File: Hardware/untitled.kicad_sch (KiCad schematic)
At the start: 16 parts, among them IC1 LM74502HDDFR, J3 CarLVPowerConnector, Q12 PSMN8R5-40MSDX

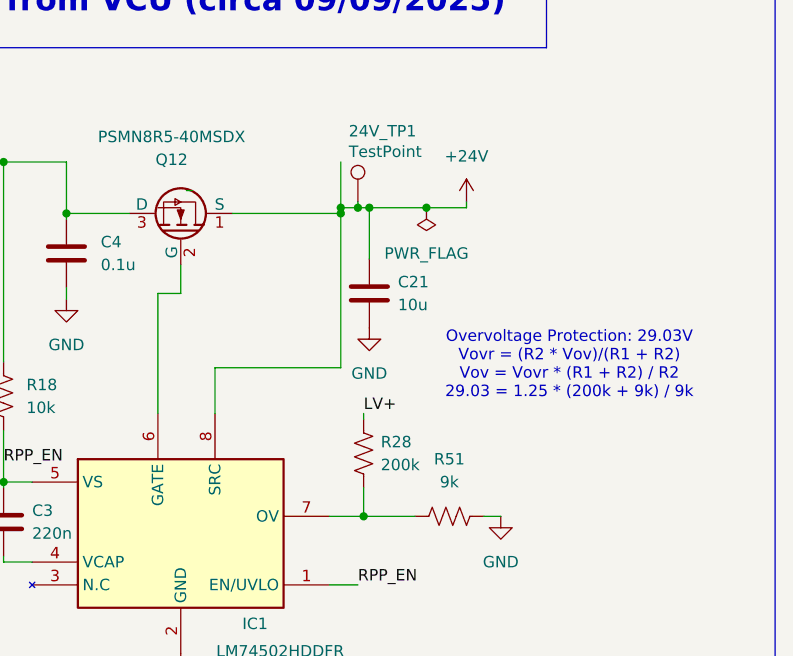
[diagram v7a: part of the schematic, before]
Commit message: added BOM
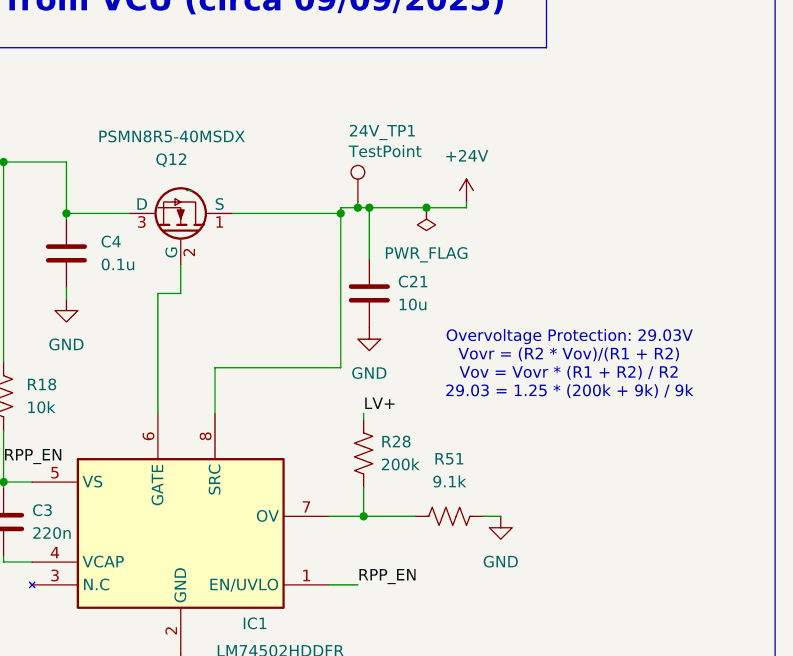
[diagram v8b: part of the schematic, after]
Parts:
- 24V_TP1, LVGND_TP1, LVPRW_TP2: now left out of the parts list
- 3.3V_In1, J3: Manufactuerer (none) -> Molex; P/N (none) -> 105309-1102
- C20: Manufactuerer (none) -> TAIYO YUDEN; P/N C0805C105K5PACTU -> MLASU168SB5105KTNA01
- C21: Manufactuerer (none) -> Murata Electronics; P/N (none) -> GRM21BR61H106KE43K
- C3: Manufactuerer KYOCERA AVX -> TAIYO YUDEN; P/N 06035C223K4T4A -> MSASU168SB7224KTNB25
- D12: Manufactuerer (none) -> Comchip Technology; P/N (none) -> CDBC560-G
- IC1: Manufactuerer (none) -> Texas Instruments; P/N (none) -> LM74502HDDFR
- Q12: Manufactuerer (none) -> Nexperia; P/N (none) -> PSMN8R5-40MSDX
- R18: Manufactuerer (none) -> Vishay; P/N (none) -> CRCW060310K0FKEI
- R28: Manufactuerer (none) -> Vishay; P/N (none) -> MCT06030C2003FP500
- R51: value 9k -> 9.1k; Manufactuerer (none) -> Vishay; P/N (none) -> CRCW06039K10FKEC
- Z2: Manufactuerer (none) -> Micro Commercial Components (MCC); P/N (none) -> SMAF4751A-TP
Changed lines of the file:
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@@
-	)
-	(junction
-		(at 118.11 54.61)
-		(diameter 0)
-		(color 0 0 0 0)
 	)
 	(junction
@@
 		(pts
 			(xy 80.645 71.755) (xy 80.645 49.53)
-		)
-		(stroke
-			(width 0)
-			(type default)
-		)
-	)
-	(wire
-		(pts
-			(xy 118.11 49.53) (xy 118.11 54.61)
 		)
 		(stroke
@@
 			)
 		)
-		(property "Datasheet" "http://www.comchiptech.com/admin/files/product/CDBC520-HF%20Thru195217.%20CDBC5100-HF%20RevB.pdf"
+		(property "Datasheet" "https://www.mouser.com/datasheet/3/819/1/CDBC520-HF%20Thru195377.%20CDBC5100-HF%20RevB.pdf"
 			(at 69.215 -144.12 0)
 			(effects
@@
 				)
 				(justify left top)
+				(hide yes)
+			)
+		)
+		(property "Manufactuerer" "Comchip Technology "
+			(at 81.915 49.53 0)
+			(effects
+				(font
+					(size 1.27 1.27)
+				)
+				(hide yes)
+			)
+		)
+		(property "P/N" "CDBC560-G"
+			(at 81.915 49.53 0)
+			(effects
+				(font
+					(size 1.27 1.27)
+				)
 				(hide yes)
 			)
@@
 			)
 		)
-		(property "Datasheet" "https://datasheets.kyocera-avx.com/AutoMLCCKAM.pdf"
+		(property "Datasheet" "https://www.mouser.com/catalog/specsheets/Tayio_Yuden_1102023_MS_mlcc_all_e.pdf"
 			(at 80.645 89.535 0)
 			(effects
@@
 			)
 		)
-		(property "Manufactuerer" "KYOCERA AVX "
+		(property "Manufactuerer" "TAIYO YUDEN "
 			(at 80.645 89.535 0)
 			(effects
@@
 			)
 		)
-		(property "P/N" "06035C223K4T4A "
+		(property "P/N" "MSASU168SB7224KTNB25 "
 			(at 80.645 89.535 0)
 			(effects
@@
 			)
 		)
-		(property "Datasheet" "~"
+		(property "Datasheet" "https://www.vishay.com/docs/20035/dcrcwe3.pdf"
 			(at 80.645 75.565 0)
 			(effects
@@
 			)
 		)
-		(property "Manufactuerer" ""
+		(property "Manufactuerer" "Vishay "
+			(at 80.645 75.565 0)
+			(effects
+				(font
+					(size 1.27 1.27)
+				)
+				(hide yes)
+			)
+		)
+		(property "P/N" "CRCW060310K0FKEI "
 			(at 80.645 75.565 0)
 			(effects
@@
 		(unit 1)
 		(exclude_from_sim no)
-		(in_bom yes)
+		(in_bom no)
 		(on_board yes)
 		(dnp no)
@@
 			)
 		)
-		(property "Manufactuerer" ""
+		(property "Manufactuerer" "Texas Instruments "
+			(at 83.82 85.09 0)
+			(effects
+				(font
+					(size 1.27 1.27)
+				)
+				(hide yes)
+			)
+		)
+		(property "P/N" "LM74502HDDFR"
 			(at 83.82 85.09 0)
 			(effects
@@
 			)
 		)
-		(property "Manufactuerer" ""
+		(property "Manufactuerer" "Micro Commercial Components (MCC) "
+			(at 59.055 46.99 90)
+			(effects
+				(font
+					(size 1.27 1.27)
+				)
+				(hide yes)
+			)
+		)
+		(property "P/N" "SMAF4751A-TP"
 			(at 59.055 46.99 90)
 			(effects
@@
 			)
 		)
-		(property "Datasheet" "~"
+		(property "Datasheet" "https://www.mouser.com/datasheet/3/76/1/GRM21BR61H106KE43_01A.pdf"
 			(at 121.285 64.135 0)
 			(effects
@@
 			)
 		)
-		(property "Manufactuerer" ""
+		(property "Manufactuerer" "Murata Electronics "
+			(at 121.285 64.135 0)
+			(effects
+				(font
+					(size 1.27 1.27)
+				)
+				(hide yes)
+			)
+		)
+		(property "P/N" "GRM21BR61H106KE43K"
 			(at 121.285 64.135 0)
 			(effects
@@
 		(unit 1)
 		(exclude_from_sim no)
-		(in_bom yes)
+		(in_bom no)
 		(on_board yes)
 		(dnp no)
@@
 		(unit 1)
 		(exclude_from_sim no)
-		(in_bom yes)
+		(in_bom no)
 		(on_board yes)
 		(dnp no)
@@
 			)
 		)
-		(property "Datasheet" "~"
+		(property "Datasheet" "https://ds.yuden.co.jp/TYCOMPAS/or/download?pn=MLAST063SCG681JFNA01&fileType=CA"
 			(at 72.39 90.17 0)
 			(effects
@@
 			)
 		)
-		(property "Manufactuerer" ""
+		(property "Manufactuerer" "TAIYO YUDEN "
 			(at 72.39 90.17 0)
 			(effects
@@
 			)
 		)
-		(property "P/N" "C0805C105K5PACTU"
+		(property "P/N" "MLASU168SB5105KTNA01"
 			(at 72.39 90.17 0)
 			(effects
@@
 			)
 		)
+		(property "Manufactuerer" "Nexperia "
+			(at 100.33 54.61 0)
+			(effects
+				(font
+					(size 1.27 1.27)
+				)
+				(hide yes)
+			)
+		)
+		(property "P/N" "PSMN8R5-40MSDX"
+			(at 100.33 54.61 0)
+			(effects
+				(font
+					(size 1.27 1.27)
+				)
+				(hide yes)
+			)
+		)
 		(pin "2"
 		)
@@
 			)
 		)
-		(property "Datasheet" "~"
+		(property "Datasheet" "https://www.vishay.com/doc?28705"
 			(at 120.65 81.915 0)
 			(effects
@@
 			)
 		)
-		(property "Manufactuerer" ""
+		(property "Manufactuerer" "Vishay "
+			(at 120.65 81.915 0)
+			(effects
+				(font
+					(size 1.27 1.27)
+				)
+				(hide yes)
+			)
+		)
+		(property "P/N" "MCT06030C2003FP500 "
 			(at 120.65 81.915 0)
 			(effects
@@
 			)
 		)
-		(property "Datasheet" "~"
+		(property "Datasheet" "https://tools.molex.com/pdm_docs/sd/1053091102_sd.pdf"
 			(at 35.56 143.51 0)
 			(effects
@@
 			)
 		)
-		(property "Manufactuerer" ""
+		(property "Manufactuerer" "Molex "
+			(at 35.56 143.51 0)
+			(effects
+				(font
+					(size 1.27 1.27)
+				)
+				(hide yes)
+			)
+		)
+		(property "P/N" "105309-1102 "
 			(at 35.56 143.51 0)
 			(effects
@@
 			)
 		)
-		(property "Value" "9k"
+		(property "Value" "9.1k"
 			(at 130.175 85.09 90)
 			(effects
@@
 			)
 		)
-		(property "Datasheet" "~"
+		(property "Datasheet" "https://www.mouser.com/ProductDetail/Vishay/CRCW06039K10FKEC?qs=%252B6g0mu59x7KDKDaQUc8uKw%3D%3D"
 			(at 130.175 88.9 0)
 			(effects
@@
 			)
 		)
-		(property "Manufactuerer" ""
+		(property "Manufactuerer" "Vishay "
+			(at 130.175 88.9 90)
+			(effects
+				(font
+					(size 1.27 1.27)
+				)
+				(hide yes)
+			)
+		)
+		(property "P/N" "CRCW06039K10FKEC "
 			(at 130.175 88.9 90)
 			(effects
@@
 			)
 		)
-		(property "Datasheet" ""
+		(property "Datasheet" "https://tools.molex.com/pdm_docs/sd/1053091102_sd.pdf"
 			(at 41.275 67.945 0)
 			(effects
@@
 			)
 		)
-		(property "P/N" ""
+		(property "P/N" "105309-1102 "
 			(at 41.275 67.945 0)
 			(effects
@@
 			)
 		)
-		(property "Manufactuerer" ""
+		(property "Manufactuerer" "Molex "
 			(at 41.275 67.945 0)
 			(effects
